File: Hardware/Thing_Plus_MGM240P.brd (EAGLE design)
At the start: 22.9 x 58.4 mm, 170 parts, among them J1 THING_PLUS_LOGICAL, J2 USB Female Type C Connector, J3 QWIIC_RIGHT_ANGLE, J5 MICRO-SDFRICTION, Q1 20V/4.2A/52mΩ/1.4W, U1 MGM240P, U2 XC6222B331MR-G, U3 EFM32GG12B410F1024GL120, U4 MCP73831, U5 MAX17048, U6 M24C02-FMC6TG, U7 MX25R8035FZUIL0, Y1 CRYSTAL-48MHZ

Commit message: Change debugger power circuitry
Remove VDDJ jumper
Remove VDDJ net and replace with 3V3
Add DBG_WAKE net and circuitry, which controls sleep state of debugger chip
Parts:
- removed VDDJ_EN: JUMPER-SMT_2_NC_TRACE_SILK, SparkFun-Jumpers:SMT-JUMPER_2_NC_TRACE_SILK
- added D8: 120mA/40V/370mV, SparkFun-DiscreteSemi:SOD-523
- added R18: 1k, SparkFun-Resistors:0402-TIGHT
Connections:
- removed net VDDJ: C18.1, C19.1, C20.1, C21.1, C4.1, C5.1, C6.1, FB1.2, R1.2, R12.2, R14.2, R16.2, R17.2, TP1.1, U3.C6, U3.C9, U3.G3, U3.H11, U3.J11, U3.K3, U3.L4, U3.L7, U6.8, U7.3, U7.8, VDDJ_EN.1
- new net DBG_WAKE: D8.A, U3.E1, U3.E2
- net 3.3V: now also C18.1, C19.1, C20.1, C21.1, C4.1, C5.1, C6.1, FB1.2, R1.2, R12.2, R14.2, R16.2, R17.2, TP1.1, U3.C6, U3.C9, U3.G3, U3.H11, U3.J11, U3.K3, U3.L4, U3.L7, U6.8, U7.3, U7.8; no longer VDDJ_EN.2
- net GND: now also R18.1
- net V_USB: now also D8.C, R18.2
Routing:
- net VDDJ: track 25.4 -> 0.00 mm, vias 10 -> 0
- net 3.3V: track 18.7 -> 36.5 mm, vias 8 -> 17
- net DBG_WAKE: track 0.00 -> 4.65 mm, vias 0 -> 1
- net V_USB: track 55.2 -> 58.5 mm
- net GND: track 112.0 -> 113.9 mm
- added copper zone on layer 1, net 3.3V
- added copper zone on layer 16, net 3.3V
- removed copper zone on layer 1, net VDDJ
- removed copper zone on layer 15, net VDDJ
- removed copper zone on layer 16, net VDDJ

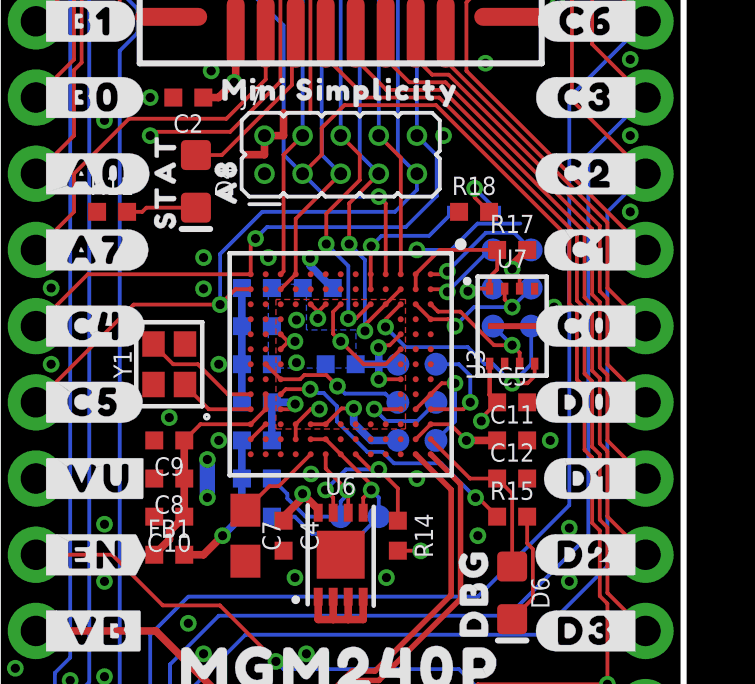
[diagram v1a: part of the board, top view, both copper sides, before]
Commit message: Design review updates
Remove VDDJ label from silk
Add jumper to debugger power control circuit for USB battery applications
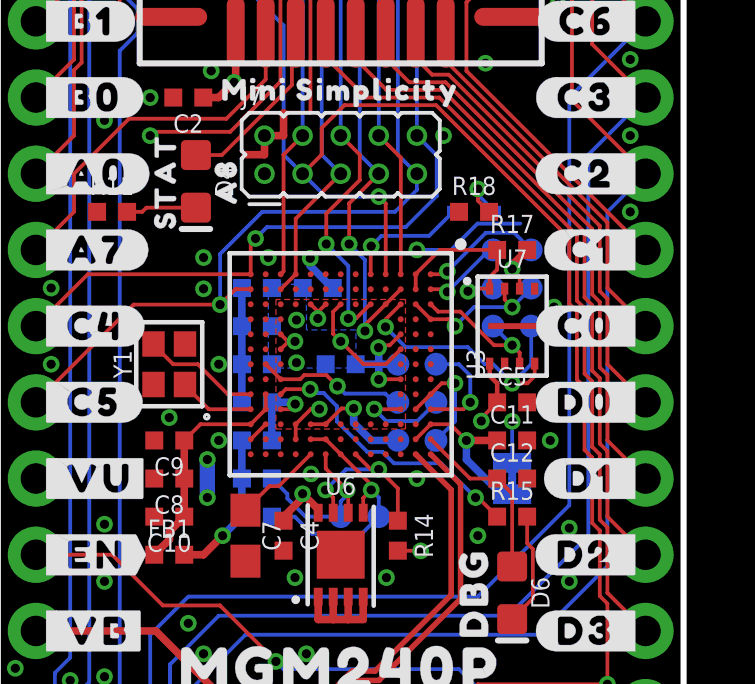
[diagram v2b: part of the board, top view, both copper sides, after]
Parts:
- removed U$65: (no value), output:#VDDJ#0
- added LP: JUMPER-SMT_2_NC_TRACE_SILK, SparkFun-Jumpers:SMT-JUMPER_2_NC_TRACE_SILK
- added U$33: (no value), output:#LP#0
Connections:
- new net N$24: D8.C, LP.1, R18.2
- net DBG_WAKE: no longer U3.E2
- net V_USB: now also LP.2; no longer D8.C, R18.2
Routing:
- net N$24: track 0.00 -> 12.0 mm, vias 0 -> 2
- net V_USB: track 58.5 -> 49.6 mm, vias 8 -> 7
- net DBG_WAKE: track 4.65 -> 4.15 mm
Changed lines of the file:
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@@
 <attribute name="VALUE" x="17.145" y="31.188" size="0.6096" layer="27" font="vector" ratio="20" align="top-center"/>
 </element>
-<element name="U$65" library="output" package="#VDDJ#0" value="" x="14.605" y="20.066" smashed="yes" rot="MR0"/>
 <element name="U$62" library="output" package="#D2_#0" value="" x="21.59" y="26.67" smashed="yes"/>
 <element name="U$77" library="output" package="#D3_#0" value="" x="21.59" y="24.13" smashed="yes"/>
@@
 <attribute name="VALUE" x="15.875" y="37.538" size="0.6096" layer="27" font="vector" ratio="20" align="top-center"/>
 </element>
+<element name="LP" library="SparkFun-Jumpers" package="SMT-JUMPER_2_NC_TRACE_SILK" package3d_urn="urn:adsk.eagle:package:39281/1" value="JUMPER-SMT_2_NC_TRACE_SILK" x="17.145" y="29.21" smashed="yes" rot="MR270">
+<attribute name="NAME" x="16.002" y="29.21" size="0.6096" layer="26" font="vector" ratio="20" rot="MR270" align="bottom-center"/>
+<attribute name="VALUE" x="18.288" y="29.21" size="0.6096" layer="28" font="vector" ratio="20" rot="MR270" align="top-center"/>
+</element>
+<element name="U$33" library="output" package="#LP#0" value="" x="16.51" y="29.21" smashed="yes" rot="MR0"/>
 </elements>
 <signals>
@@
 <wire x1="12.446" y1="30.48" x2="11.8618" y2="31.0642" width="0.254" layer="16"/>
 <contactref element="U7" pad="8"/>
-<wire x1="16.395" y1="33.04" x2="16.395" y2="32" width="0.1524" layer="1"/>
-<wire x1="16.395" y1="32" x2="16.645" y2="31.75" width="0.1524" layer="1"/>
+<wire x1="16.395" y1="33.04" x2="16.395" y2="32.635" width="0.1524" layer="1"/>
+<wire x1="16.645" y1="32.385" x2="16.395" y2="32.635" width="0.1524" layer="1"/>
+<wire x1="16.645" y1="32.385" x2="16.645" y2="31.75" width="0.1524" layer="1"/>
 <contactref element="U7" pad="3"/>
 <wire x1="16.645" y1="31.75" x2="16.11713125" y2="31.22213125" width="0.127" layer="1"/>
@@
 <vertex x="0" y="0"/>
 </polygon>
-<contactref element="R18" pad="2"/>
-<contactref element="D8" pad="C"/>
-<via x="15.89486875" y="38.88186875" extent="1-16" drill="0.3048"/>
-<wire x1="16.575" y1="38.1" x2="16.575" y2="38.2017375" width="0.127" layer="16"/>
-<wire x1="16.575" y1="38.2017375" x2="15.89486875" y2="38.88186875" width="0.127" layer="16"/>
-<wire x1="15.89486875" y1="38.88186875" x2="15.89486875" y2="38.58013125" width="0.127" layer="1"/>
-<wire x1="15.89486875" y1="38.58013125" x2="16.375" y2="38.1" width="0.127" layer="1"/>
 <wire x1="1.27" y1="29.21" x2="9.525" y2="29.21" width="0.254" layer="15"/>
 <wire x1="10.414" y1="30.099" x2="9.525" y2="29.21" width="0.254" layer="15"/>
-<wire x1="15.621" y1="30.48" x2="15.4305" y2="30.2895" width="0.254" layer="15"/>
-<wire x1="15.4305" y1="30.2895" x2="15.24" y2="30.099" width="0.254" layer="15"/>
+<wire x1="15.621" y1="30.48" x2="15.24" y2="30.099" width="0.254" layer="15"/>
 <wire x1="15.24" y1="30.099" x2="10.414" y2="30.099" width="0.254" layer="15"/>
-<wire x1="15.89486875" y1="38.88186875" x2="16.51" y2="38.2667375" width="0.254" layer="15"/>
-<wire x1="16.51" y1="31.48834375" x2="16.65053125" y2="31.3478125" width="0.254" layer="15"/>
-<wire x1="16.65053125" y1="31.3478125" x2="16.65053125" y2="30.905925" width="0.254" layer="15"/>
-<wire x1="16.65053125" y1="30.905925" x2="16.338075" y2="30.59346875" width="0.254" layer="15"/>
-<wire x1="15.73446875" y1="30.59346875" x2="15.621" y2="30.48" width="0.254" layer="15"/>
-<wire x1="16.338075" y1="30.59346875" x2="15.73446875" y2="30.59346875" width="0.254" layer="15"/>
-<wire x1="16.51" y1="38.2667375" x2="16.51" y2="31.48834375" width="0.254" layer="15"/>
+<contactref element="LP" pad="2"/>
+<wire x1="17.145" y1="28.6893" x2="16.7767" y2="28.6893" width="0.254" layer="16"/>
+<wire x1="15.621" y1="29.845" x2="15.621" y2="30.48" width="0.254" layer="16"/>
+<wire x1="16.7767" y1="28.6893" x2="15.621" y2="29.845" width="0.254" layer="16"/>
 </signal>
 <signal name="V_BATT">
@@
 </signal>
 <signal name="DBG_WAKE">
-<contactref element="U3" pad="E2"/>
 <contactref element="D8" pad="A"/>
 <contactref element="U3" pad="E1"/>
-<wire x1="12.43" y1="35.52" x2="12.43" y2="36.02" width="0.127" layer="1"/>
 <wire x1="12.43" y1="36.02" x2="12.43" y2="36.941" width="0.127" layer="1"/>
 <wire x1="12.43" y1="36.941" x2="12.446" y2="36.957" width="0.127" layer="1"/>
@@
 <wire x1="15.175" y1="38.1" x2="14.3749" y2="37.2999" width="0.127" layer="16"/>
 </signal>
+<signal name="N$24">
+<contactref element="R18" pad="2"/>
+<contactref element="LP" pad="1"/>
+<contactref element="D8" pad="C"/>
+<wire x1="17.145" y1="29.7307" x2="17.145" y2="31.115" width="0.127" layer="16"/>
+<via x="17.145" y="31.115" extent="1-16" drill="0.3048"/>
+<wire x1="17.145" y1="31.115" x2="17.78" y2="31.75" width="0.127" layer="15"/>
+<wire x1="17.78" y1="37.084" x2="16.002" y2="38.862" width="0.127" layer="15"/>
+<via x="16.002" y="38.862" extent="1-16" drill="0.3048"/>
+<wire x1="16.002" y1="38.862" x2="16.002" y2="38.673" width="0.127" layer="16"/>
+<wire x1="16.002" y1="38.673" x2="16.575" y2="38.1" width="0.127" layer="16"/>
+<wire x1="17.78" y1="31.75" x2="17.78" y2="37.084" width="0.127" layer="15"/>
+<wire x1="16.002" y1="38.862" x2="16.002" y2="38.473" width="0.127" layer="1"/>
+<wire x1="16.002" y1="38.473" x2="16.375" y2="38.1" width="0.127" layer="1"/>
+</signal>
 </signals>

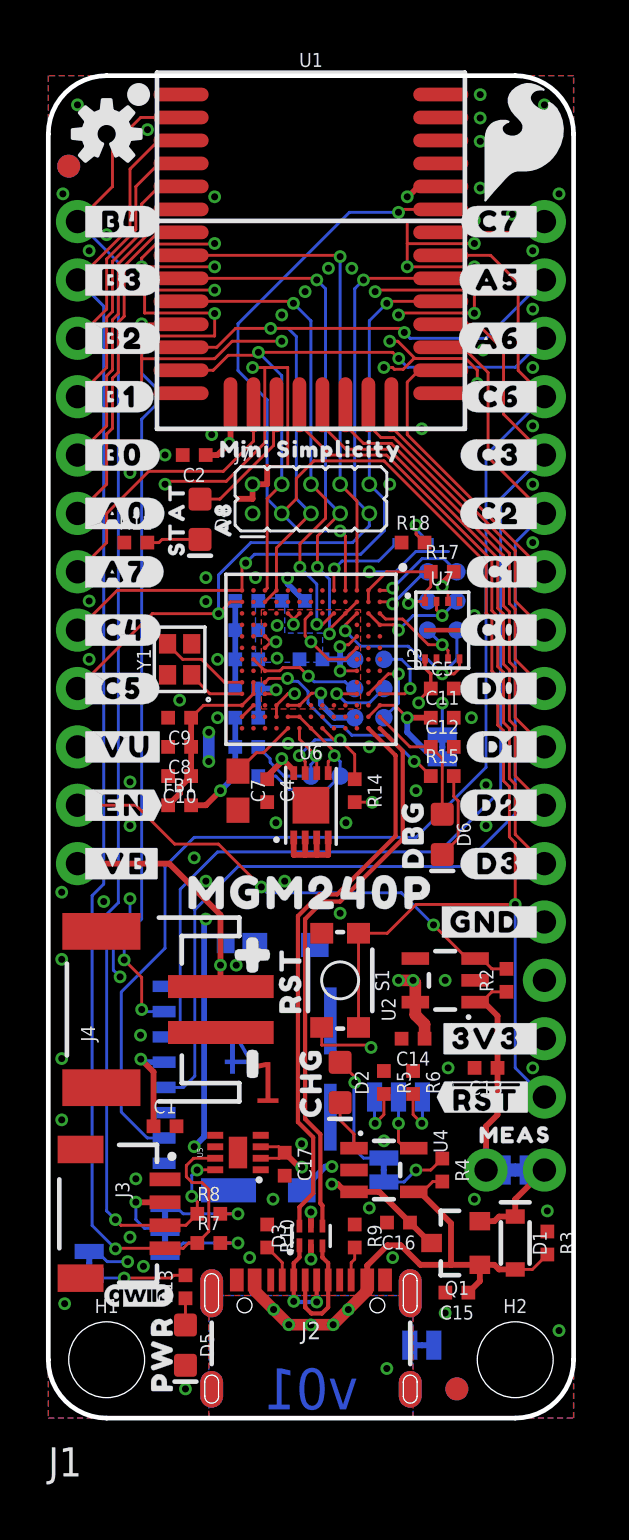
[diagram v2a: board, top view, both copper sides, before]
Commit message: Testing fixes
Update version number to v02
Mirror MX8035 footprint (whoops...)
Swap R15 for 2k2 (turns out VREGO is 3V3, not 5V)
Add trace to 3V3 pour to connect between V_USB and N$24
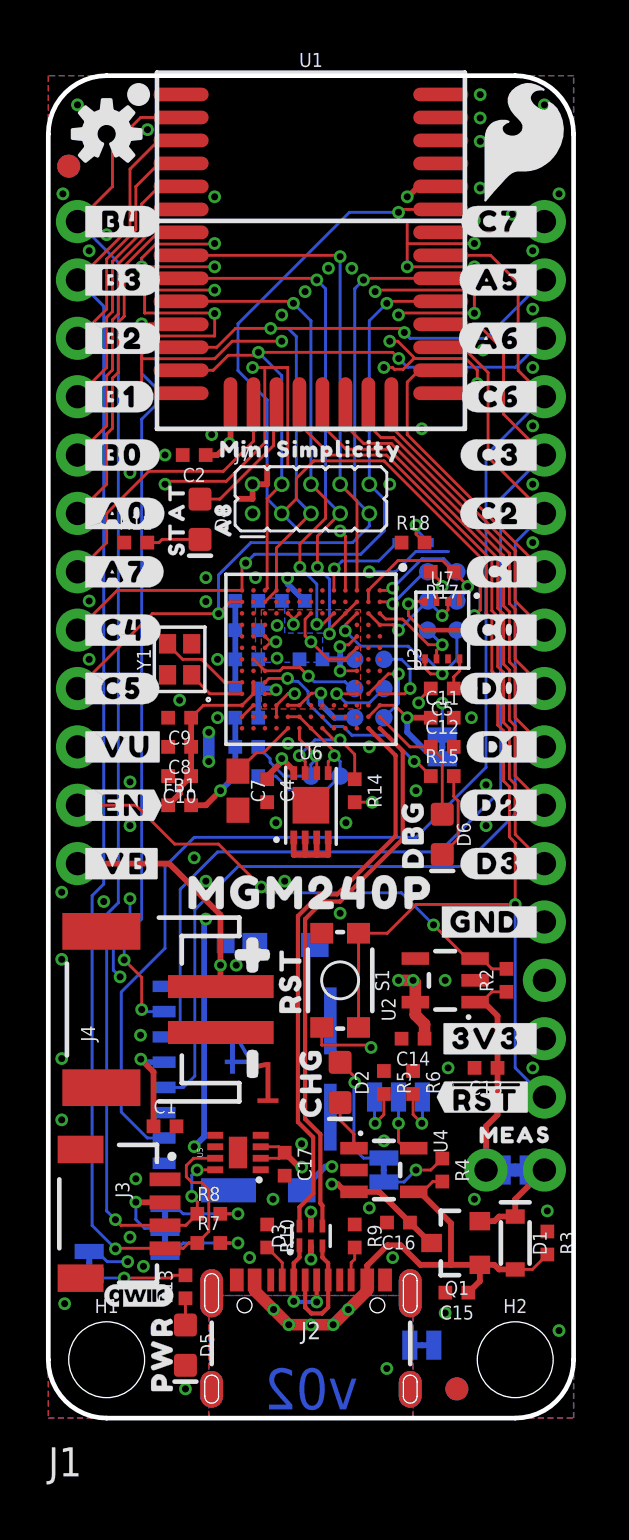
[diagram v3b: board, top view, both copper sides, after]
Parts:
- R15: value 4.7k -> 2.2k
- moved TP10 1.27 mm to (17.8, 35.6)
- moved TP8 1.27 mm to (16.5, 35.6)
- turned C5 to 180 degrees
- turned R17 to 180 degrees
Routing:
- net GND: track 113.9 -> 122.2 mm, vias 112 -> 114
- net 3.3V: track 36.5 -> 37.7 mm
- net DBG_CS: track 6.59 -> 7.48 mm
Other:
- board text added: "v02"
- board text removed: "v01"

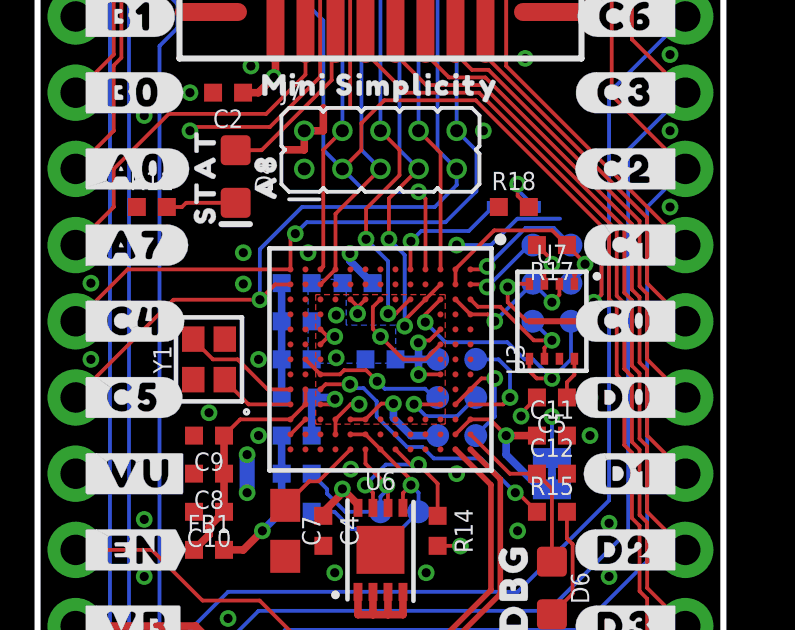
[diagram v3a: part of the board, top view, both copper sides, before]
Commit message: Design review updates
Adjust DBG_SCK trace
Remove extra GND trace of C6
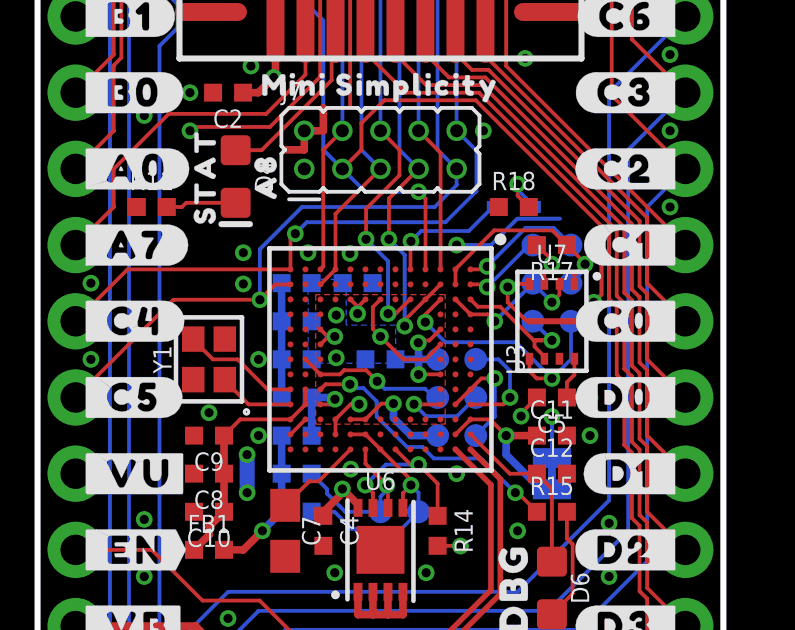
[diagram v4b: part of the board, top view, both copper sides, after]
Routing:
- net GND: track 122.2 -> 120.9 mm
- net DBG_SCK: track 4.90 -> 5.51 mm
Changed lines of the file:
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@@
 <via x="10.4394" y="29.3624" extent="1-16" drill="0.3048"/>
 <contactref element="R18" pad="1"/>
-<wire x1="11.168" y1="35.56" x2="11.1541125" y2="35.56" width="0.254" layer="16"/>
-<wire x1="11.1541125" y1="35.56" x2="10.414" y2="36.3001125" width="0.254" layer="16"/>
-<wire x1="10.414" y1="36.5506" x2="10.414" y2="36.3001125" width="0.254" layer="16"/>
 <wire x1="13.97" y1="36.83" x2="15.113" y2="36.83" width="0.127" layer="16"/>
 <wire x1="15.9925" y1="37.7095" x2="17.418" y2="37.7095" width="0.127" layer="16"/>
@@
 <wire x1="16.53954375" y1="33.655" x2="15.42054375" y2="34.774" width="0.127" layer="1"/>
 <wire x1="15.42054375" y1="34.774" x2="14.676" y2="34.774" width="0.127" layer="1"/>
-<wire x1="16.895" y1="33.04" x2="16.895" y2="33.405" width="0.127" layer="1"/>
-<wire x1="16.895" y1="33.405" x2="17.145" y2="33.655" width="0.127" layer="1"/>
+<wire x1="16.5648" y1="33.655" x2="16.5648" y2="33.4464" width="0.127" layer="1"/>
+<wire x1="16.895" y1="33.04" x2="16.895" y2="33.1162" width="0.127" layer="1"/>
+<wire x1="16.895" y1="33.1162" x2="16.5648" y2="33.4464" width="0.127" layer="1"/>
+<wire x1="16.5648" y1="33.655" x2="17.145" y2="33.655" width="0.127" layer="1"/>
 </signal>
 <signal name="DBG_POCI">
@@
 <wire x1="17.145" y1="32.385" x2="17.78" y2="33.02" width="0.127" layer="16"/>
 <wire x1="17.78" y1="33.02" x2="17.78" y2="34.29" width="0.127" layer="16"/>
-<wire x1="17.145" y1="32.385" x2="16.51" y2="33.02" width="0.127" layer="16"/>
 <wire x1="13.5917" y1="33.5915" x2="12.9236" y2="34.2596" width="0.127" layer="16"/>
-<wire x1="16.2342125" y1="33.02" x2="15.6627125" y2="33.5915" width="0.127" layer="16"/>
-<wire x1="15.6627125" y1="33.5915" x2="13.5917" y2="33.5915" width="0.127" layer="16"/>
-<wire x1="16.51" y1="33.02" x2="16.2342125" y2="33.02" width="0.127" layer="16"/>
+<wire x1="17.145" y1="32.385" x2="15.9385" y2="33.5915" width="0.127" layer="16"/>
+<wire x1="15.9385" y1="33.5915" x2="13.5917" y2="33.5915" width="0.127" layer="16"/>
 <wire x1="16.395" y1="33.04" x2="16.395" y2="32.627" width="0.127" layer="1"/>
 <wire x1="16.637" y1="32.385" x2="17.145" y2="32.385" width="0.127" layer="1"/>

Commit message: Flip DBG TX and RX
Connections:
- net DBG_RX: now also TP13.1, U3.A1; no longer TP14.1, U3.A2
- net DBG_TX: now also TP14.1, U3.A2; no longer TP13.1, U3.A1
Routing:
- net DBG_TX: track 4.16 -> 2.69 mm
- net DBG_RX: track 2.69 -> 4.16 mm
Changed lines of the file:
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@@
 <wire x1="17.08" y1="50.6" x2="19.25" y2="50.6" width="0.127" layer="1"/>
 </signal>
-<signal name="DBG_TX">
+<signal name="DBG_RX">
 <contactref element="U3" pad="A1"/>
 <contactref element="TP13" pad="1"/>
@@
 <wire x1="16.2687" y1="37.4015" x2="17.2085" y2="37.4015" width="0.127" layer="16"/>
 </signal>
-<signal name="DBG_RX">
+<signal name="DBG_TX">
 <contactref element="U3" pad="A2"/>
 <contactref element="TP14" pad="1"/>
